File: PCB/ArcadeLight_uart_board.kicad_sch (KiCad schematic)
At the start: 20 parts, among them J1 Partition_Lights_L, J10 Circle_LED, J11 Cross_LED, J12 Square_LED, J13 Triangle_LED, J3 12V_In, J9 Partition_Lights_R, P7 CONN_01X01, P9 CONN_01X01, Q1 AO3404A, Q2 IRFR9024N, U2 ULN2003, U6 ULN2003

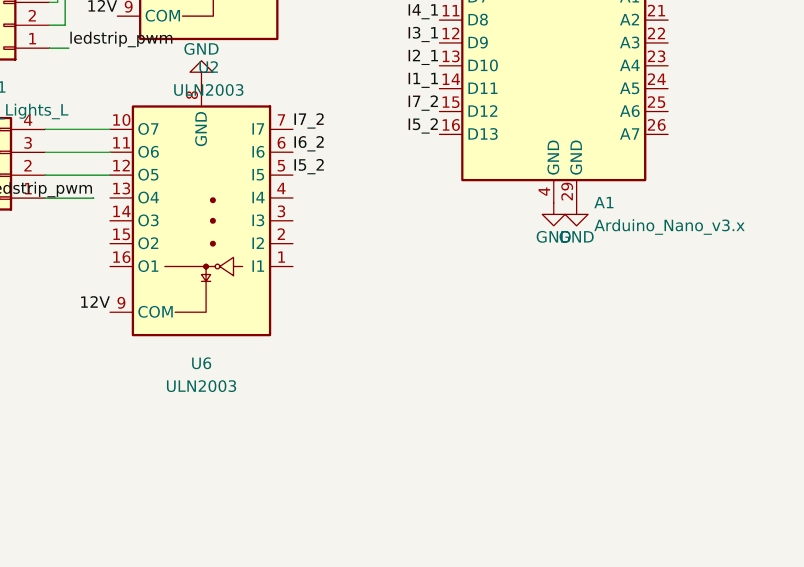
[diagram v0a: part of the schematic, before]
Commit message: Arduino program PWM brightness control added
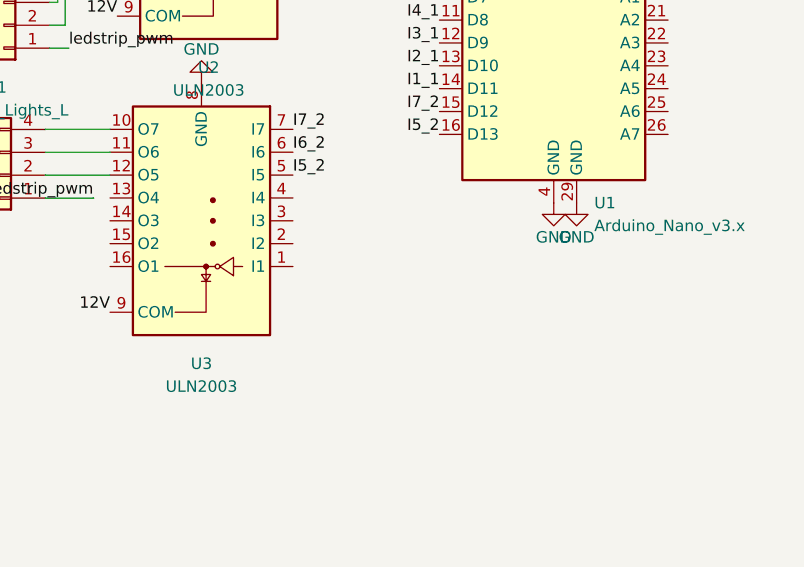
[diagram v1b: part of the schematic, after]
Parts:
- renumbered A1 to U1, U6 to U3
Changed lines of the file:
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@@
   (symbol (lib_id "MCU_Module:Arduino_Nano_v3.x") (at 203.3581 112.1521 0) (unit 1)
     (in_bom yes) (on_board yes) (dnp no) (fields_autoplaced)
-    (property "Reference" "A1" (at 207.854 137.5521 0)
+    (property "Reference" "U1" (at 207.854 137.5521 0)
       (effects (font (size 1.27 1.27)) (justify left))
     )
@@
       (project "ArcadeLight_uart_board"
         (path "/07e2c1ee-0df3-4731-a138-2d4ed34e257e"
-          (reference "A1") (unit 1)
+          (reference "U1") (unit 1)
         )
       )
@@
   (symbol (lib_id "Transistor_Array:ULN2003") (at 164.2167 139.5333 180) (unit 1)
     (in_bom yes) (on_board yes) (dnp no) (fields_autoplaced)
-    (property "Reference" "U6" (at 164.2167 155.4083 0)
+    (property "Reference" "U3" (at 164.2167 155.4083 0)
       (effects (font (size 1.27 1.27)))
     )
@@
       (project "ArcadeLight_uart_board"
         (path "/07e2c1ee-0df3-4731-a138-2d4ed34e257e"
-          (reference "U6") (unit 1)
-        )
-      )
+          (reference "U3") (unit 1)
+        )
+      )

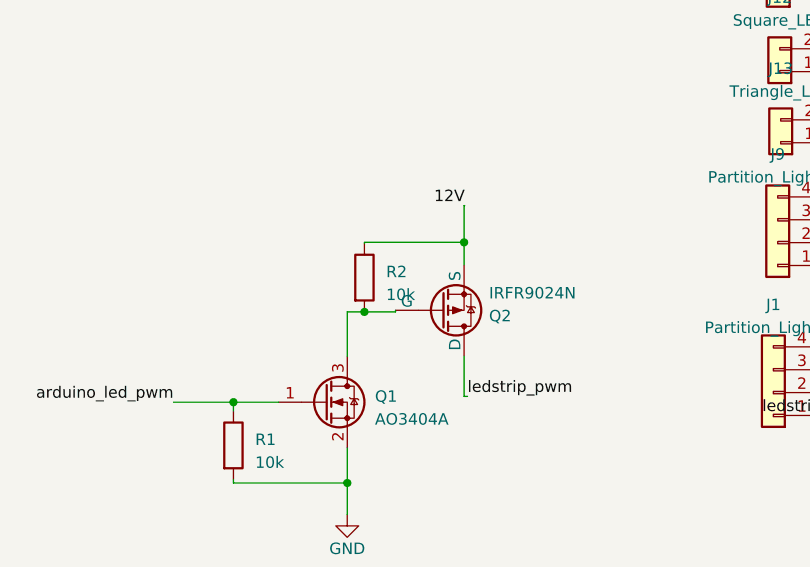
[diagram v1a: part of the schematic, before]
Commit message: R1 fix to 1k
10k do not work
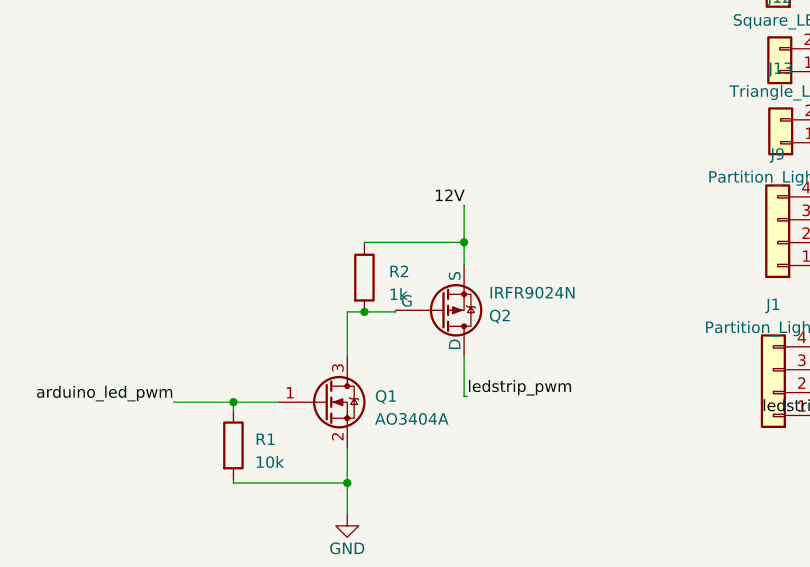
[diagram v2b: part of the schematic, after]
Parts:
- R2: value 10k -> 1k
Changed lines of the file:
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@@
   (symbol (lib_id "Device:R") (at 96.3422 121.6914 0) (unit 1)
     (in_bom yes) (on_board yes) (dnp no) (fields_autoplaced)
-    (property "Reference" "R2" (at 98.7552 121.0564 0)
+    (property "Reference" "R2" (at 99.06 121.0564 0)
       (effects (font (size 1.27 1.27)) (justify left))
     )
-    (property "Value" "10k" (at 98.7552 123.5964 0)
+    (property "Value" "1k" (at 99.06 123.5964 0)
       (effects (font (size 1.27 1.27)) (justify left))
     )

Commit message: Readme update
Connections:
- net I6_2 is gone; now on an unnamed net: U3.6 (I6)
- net I1_1: no longer names the net of U1.14 (D11), U2.1 (I1)
- net I2_1: no longer names the net of U1.13 (D10), U2.2 (I2)
- net I3_1: no longer names the net of U1.12 (D9), U2.3 (I3)
- net I4_1: no longer names the net of U1.11 (D8), U2.4 (I4)
- net I5_1: no longer names the net of U1.10 (D7), U2.5 (I5)
- net I5_2: no longer names the net of U1.16 (D13), U3.5 (I5)
- net I6_1: no longer names the net of U1.9 (D6), U2.6 (I6)
- net I7_1: no longer names the net of U1.8 (D5), U2.7 (I7)
- net I7_2: no longer names the net of U1.15 (D12), U3.7 (I7)
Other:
- moved on the sheet: J1, J10, J11, J12, J13, J3, J9, JP1, JP2, JP3, JP4, P7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
